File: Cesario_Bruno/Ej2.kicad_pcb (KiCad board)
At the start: 2 copper layers, 16 parts, among them P1 CONN_01X14, P2 CONN_01X14, U1 SN74LVC1GX04, U2 74HCT4053, U3 LTC5507, X1 XTAL

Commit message: Prueba de Ruteo PCB ambas capas. Finalizado.
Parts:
- C1, C2, C3, C4, C5, C6, R1, R2, R3, U1, U2, U3: moved to B.Cu
- PTC1: footprint Ej2:C_0805_HandSoldering -> Ej2:R_0805_HandSoldering; moved to B.Cu
- moved X1 60.9 mm to (163.8, 70.9), turned to 0 degrees
- moved R3 60.2 mm to (185.5, 86.0), turned to 270 degrees
- moved C2 59.2 mm to (182.6, 93.0), turned to 270 degrees
- moved P1 52.8 mm to (168.0, 80.0)
- moved C3 45.1 mm to (177.6, 91.5)
- moved C4 38.6 mm to (153.8, 84.4)
- moved PTC1 38.5 mm to (179.8, 86.3)
- moved C1 36.9 mm to (166.2, 92.7), turned to 180 degrees
- moved R1 36.2 mm to (173.5, 86.4)
- moved C5 35.8 mm to (166.1, 87.0)
- moved R2 35.3 mm to (160.4, 89.5)
- moved U2 34.2 mm to (152.9, 91.4), turned to 270 degrees
- moved U3 29.1 mm to (159.5, 84.0), turned to 270 degrees
- moved U1 25.3 mm to (158.1, 93.7)
- moved C6 23.8 mm to (172.0, 92.0), turned to 180 degrees
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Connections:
- PTC1 pad 1: (no net) -> /ArduinoCon/PTC
- PTC1 pad 2: (no net) -> GND
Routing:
- net GND: track 0.00 -> 74.0 mm, vias 0 -> 4
- net /ArduinoCon/ENVELOPE_IN: track 0.00 -> 70.6 mm, vias 0 -> 2
- net /ArduinoCon/FREQUENCY_IN: track 0.00 -> 53.6 mm
- net /OSC_DRIVER/Switch_IN-: track 0.00 -> 51.8 mm, vias 0 -> 2
- net +5V: track 0.00 -> 47.8 mm, vias 0 -> 2
- net +3V3: track 0.00 -> 40.4 mm, vias 0 -> 4
- net /SWITCH_ENVELOPE/xtal_N: track 0.00 -> 38.3 mm, vias 0 -> 1
- net /ArduinoCon/PTC: track 0.00 -> 32.4 mm, vias 0 -> 2
- net /SWITCH_ENVELOPE/xtal_P: track 0.00 -> 28.4 mm, vias 0 -> 1
- net Net-(R2-Pad1): track 0.00 -> 27.6 mm, vias 0 -> 2
- net /ArduinoCon/DIG_CONTROL: track 0.00 -> 25.7 mm, vias 0 -> 2
- net /OSC_DRIVER/Switch_IN+: track 0.00 -> 19.8 mm, vias 0 -> 2
- net Net-(C4-Pad1): track 0.00 -> 12.0 mm
- net Net-(C5-Pad2): track 0.00 -> 8.52 mm
- net Net-(C4-Pad2): track 0.00 -> 5.34 mm
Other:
- board outline added: 39.2 x 36 mm

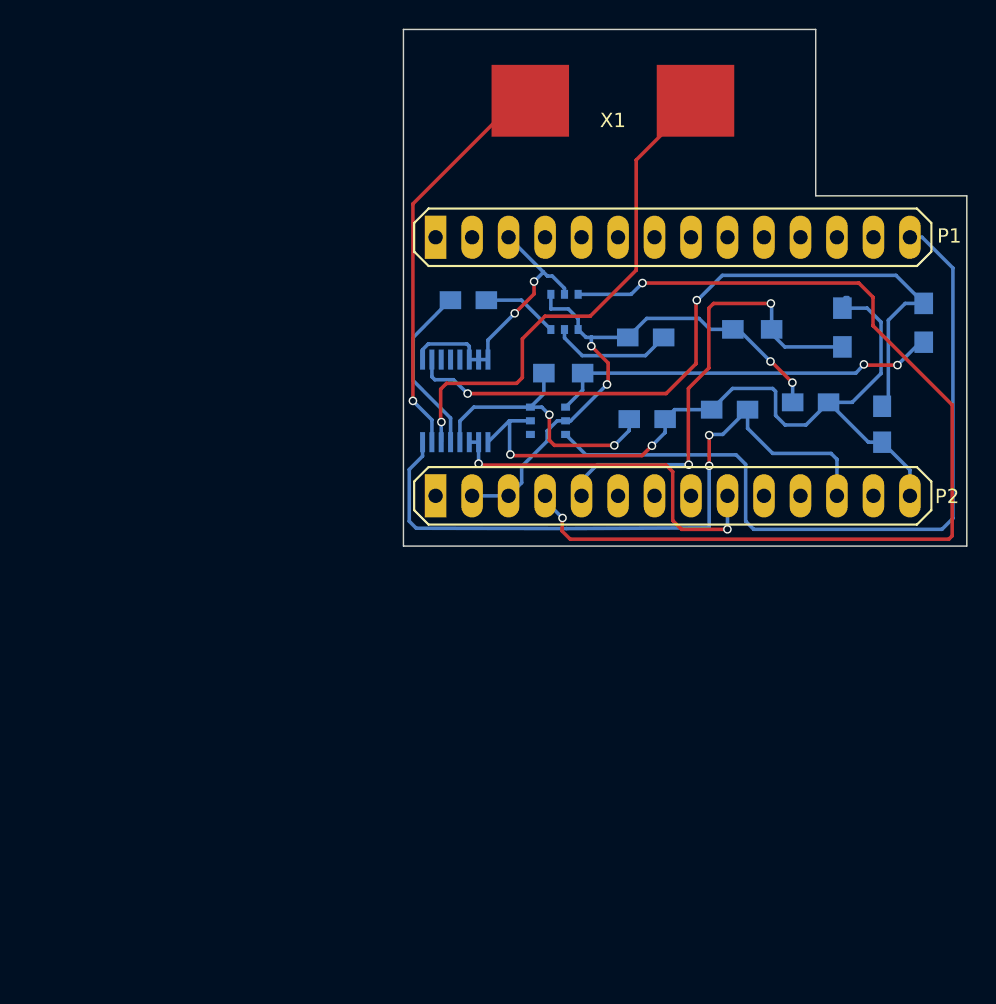
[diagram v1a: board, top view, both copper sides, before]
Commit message: Modificacion para inclusion de plantilla.
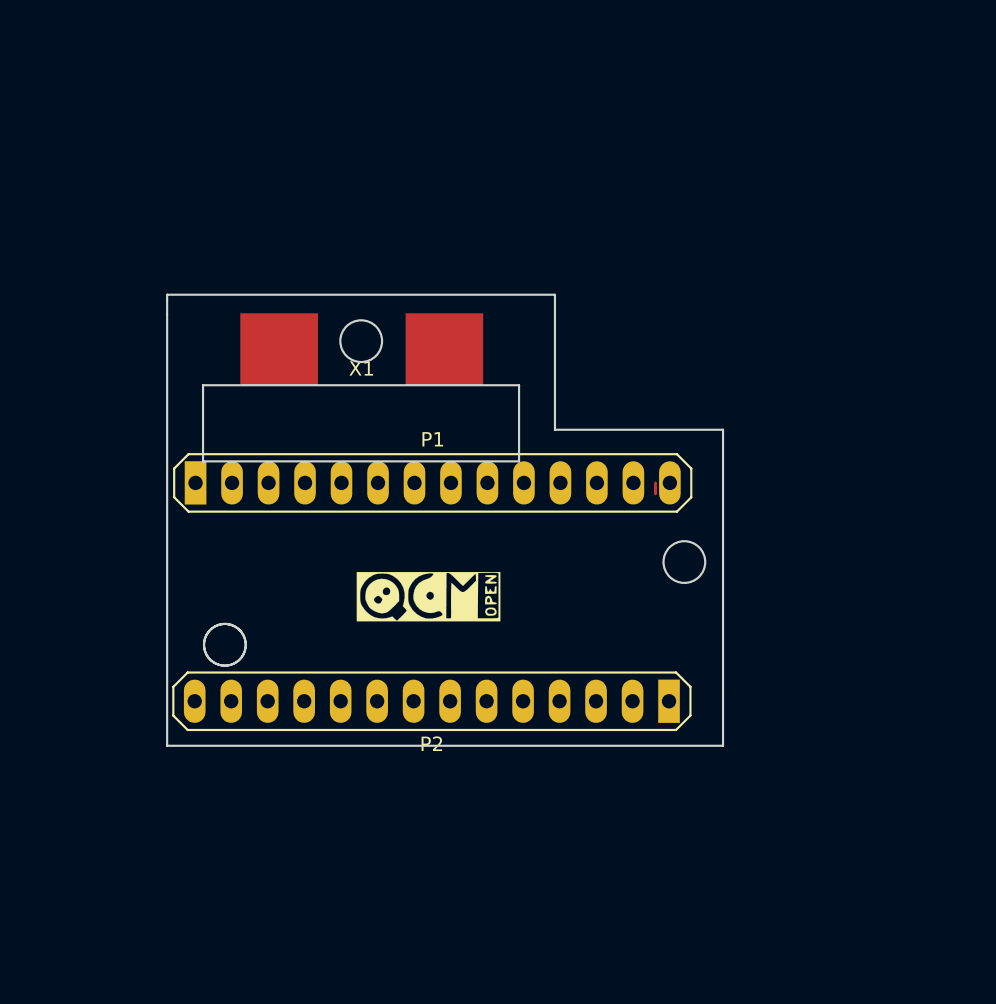
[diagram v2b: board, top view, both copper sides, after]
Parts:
- removed C1, C2: 33pF, Ej2:C_0805_HandSoldering
- removed C3, C6: 100nF, Ej2:C_0805_HandSoldering
- removed C4, C5: pF, Ej2:C_0805_HandSoldering
- removed PTC1: PTC_HandSoldering, Ej2:R_0805_HandSoldering
- removed R1, R3: 1K, Ej2:R_0805_HandSoldering
- removed R2: 2M2, Ej2:R_0805_HandSoldering
- removed U1: SN74LVC1GX04, Ej2:SOT-23-6
- removed U2: 74HCT4053, Ej2:TSSOP16
- removed U3: LTC5507, Ej2:SOT-23-6
- added G***: LOGO, OpenQCM:openQCM, F.Cu at (151.0, 105.0)
- P1, P2: footprint Ej2:PINHEAD1-14 -> OpenQCM:PINHEAD1-14
- X1: footprint Ej2:XTAL_con -> OpenQCM:XTAL_con
- moved X1 24.6 mm to (146.3, 88.2)
- moved P1 23.9 mm to (151.3, 97.1)
- moved P2 22.0 mm to (151.2, 112.3), turned to 180 degrees
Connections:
- P1 pad 1: Net-(P1-Pad1) -> (no net)
- P1 pad 10: Net-(P1-Pad10) -> (no net)
- P1 pad 11: Net-(P1-Pad11) -> (no net)
- P1 pad 12: Net-(P1-Pad12) -> (no net)
- P1 pad 13: Net-(P1-Pad13) -> (no net)
- P1 pad 14: /ArduinoCon/FREQUENCY_IN -> /Arduino/FREQUENCY_IN
- P1 pad 2: Net-(P1-Pad2) -> (no net)
- P1 pad 4: Net-(P1-Pad4) -> (no net)
- P1 pad 5: Net-(P1-Pad5) -> (no net)
- P1 pad 6: Net-(P1-Pad6) -> (no net)
- P1 pad 7: Net-(P1-Pad7) -> (no net)
- P1 pad 8: Net-(P1-Pad8) -> (no net)
- P1 pad 9: Net-(P1-Pad9) -> (no net)
- P2 pad 1: Net-(P2-Pad1) -> (no net)
- P2 pad 10: Net-(P2-Pad10) -> (no net)
- P2 pad 11: Net-(P2-Pad11) -> (no net)
- P2 pad 13: Net-(P2-Pad13) -> (no net)
- P2 pad 4: /ArduinoCon/ENVELOPE_IN -> /Arduino/ENVELOPE_IN
- P2 pad 5: /ArduinoCon/PTC -> /Arduino/PTC
- P2 pad 6: Net-(P2-Pad6) -> (no net)
- P2 pad 7: Net-(P2-Pad7) -> (no net)
- P2 pad 8: Net-(P2-Pad8) -> (no net)
- P2 pad 9: /ArduinoCon/DIG_CONTROL -> /Arduino/DIG_CONTROL
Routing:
- net GND: track 74.0 -> 0.00 mm, vias 4 -> 0
- net /ArduinoCon/ENVELOPE_IN: track 70.6 -> 0.00 mm, vias 2 -> 0
- net /ArduinoCon/FREQUENCY_IN: track 53.6 -> 0.00 mm
- net /OSC_DRIVER/Switch_IN-: track 51.8 -> 0.00 mm, vias 2 -> 0
- net +5V: track 47.8 -> 0.00 mm, vias 2 -> 0
- net +3V3: track 40.4 -> 0.00 mm, vias 4 -> 0
- net /SWITCH_ENVELOPE/xtal_N: track 38.3 -> 0.00 mm, vias 1 -> 0
- net /ArduinoCon/PTC: track 32.4 -> 0.00 mm, vias 2 -> 0
- net /SWITCH_ENVELOPE/xtal_P: track 28.4 -> 0.00 mm, vias 1 -> 0
- net Net-(R2-Pad1): track 27.6 -> 0.00 mm, vias 2 -> 0
- net /ArduinoCon/DIG_CONTROL: track 25.7 -> 0.00 mm, vias 2 -> 0
- net /OSC_DRIVER/Switch_IN+: track 19.8 -> 0.00 mm, vias 2 -> 0
- net Net-(C4-Pad1): track 12.0 -> 0.00 mm
- net Net-(C5-Pad2): track 8.52 -> 0.00 mm
- net Net-(C4-Pad2): track 5.34 -> 0.00 mm
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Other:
- board size 39.2 x 36 mm -> 38.7 x 31.4 mm
- net class Default: trace_width 0.25 -> 0.2032
- net class PW added: clearance 0.2, trace_width 0.5, via_dia 0.6, via_drill 0.4
- rule pad_to_mask_clearance: 0 -> 0.2
- rule trace_min: 0.2 -> 0.2032

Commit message: Fin Clase 3. Generacion Nuevo PCB y Ruteo. Capa de Cobre. Archivos Gerber y Visualización.
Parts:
- removed the G*** at (151.0, 105.0)
- added C1: 33pF, Ej2:C_0603_HandSoldering, B.Cu at (145.8, 104.1)
- added C2: 33pF, Ej2:C_0603_HandSoldering, B.Cu at (155.3, 108.1)
- added C3: 100nF, Ej2:C_0603_HandSoldering, B.Cu at (148.4, 100.7)
- added C4: pF, Ej2:C_0603_HandSoldering, B.Cu at (158.9, 108.2)
- added C5: pF, Ej2:C_0603_HandSoldering, B.Cu at (162.6, 105.7)
- added C6: 100nF, Ej2:C_0603_HandSoldering, B.Cu at (162.8, 109.3)
- added G***: LOGO, Ej2:openQCM, F.Cu at (151.4, 103.0)
- added PTC1: PTC_HandSoldering, Ej2:R_0805_HandSoldering, B.Cu at (153.0, 103.7)
- added R1: 1K, Ej2:R_0805_HandSoldering, B.Cu at (157.4, 102.8)
- added R2: 2M2, Ej2:R_0805_HandSoldering, B.Cu at (145.9, 109.0)
- added R3: 1K, Ej2:R_0805_HandSoldering, B.Cu at (151.9, 109.0)
- added U1: SN74LVC1GX04, Ej2:SOT-23-6, B.Cu at (162.2, 102.7)
- added U2: 74HCT4053, Ej2:TSSOP16, B.Cu at (141.3, 103.7)
- added U3: LTC5507, Ej2:SOT-23-6, B.Cu at (168.0, 108.3)
- P1, P2: footprint OpenQCM:PINHEAD1-14 -> Ej2:PINHEAD1-14
- X1: footprint OpenQCM:XTAL_con -> Ej2:XTAL_con; moved to B.Cu
- moved X1 2.16 mm to (147.6, 86.4)
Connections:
- P1 pad 1: (no net) -> Net-(P1-Pad1)
- P1 pad 10: (no net) -> Net-(P1-Pad10)
- P1 pad 11: (no net) -> Net-(P1-Pad11)
- P1 pad 12: (no net) -> Net-(P1-Pad12)
- P1 pad 13: (no net) -> Net-(P1-Pad13)
- P1 pad 14: /Arduino/FREQUENCY_IN -> /ArduinoCon/FREQUENCY_IN
- P1 pad 2: (no net) -> Net-(P1-Pad2)
- P1 pad 4: (no net) -> Net-(P1-Pad4)
- P1 pad 5: (no net) -> Net-(P1-Pad5)
- P1 pad 6: (no net) -> Net-(P1-Pad6)
- P1 pad 7: (no net) -> Net-(P1-Pad7)
- P1 pad 8: (no net) -> Net-(P1-Pad8)
- P1 pad 9: (no net) -> Net-(P1-Pad9)
- P2 pad 1: (no net) -> Net-(P2-Pad1)
- P2 pad 10: (no net) -> Net-(P2-Pad10)
- P2 pad 11: (no net) -> Net-(P2-Pad11)
- P2 pad 13: (no net) -> Net-(P2-Pad13)
- P2 pad 4: /Arduino/ENVELOPE_IN -> /ArduinoCon/ENVELOPE_IN
- P2 pad 5: /Arduino/PTC -> /ArduinoCon/PTC
- P2 pad 6: (no net) -> Net-(P2-Pad6)
- P2 pad 7: (no net) -> Net-(P2-Pad7)
- P2 pad 8: (no net) -> Net-(P2-Pad8)
- P2 pad 9: /Arduino/DIG_CONTROL -> /ArduinoCon/DIG_CONTROL
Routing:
- net /SWITCH_ENVELOPE/xtal_P: track 0.00 -> 55.6 mm
- net +3V3: track 0.00 -> 49.3 mm
- net /SWITCH_ENVELOPE/xtal_N: track 0.00 -> 48.8 mm
- net GND: track 0.00 -> 37.5 mm, vias 0 -> 4
- net +5V: track 0.00 -> 35.3 mm
- net Net-(R2-Pad1): track 0.00 -> 31.8 mm, vias 0 -> 2
- net Net-(C4-Pad1): track 0.00 -> 30.4 mm
- net /OSC_DRIVER/Switch_IN+: track 0.00 -> 27.9 mm, vias 0 -> 4
- net /OSC_DRIVER/Switch_IN-: track 0.00 -> 19.5 mm, vias 0 -> 2
- net /ArduinoCon/PTC: track 0.00 -> 15.9 mm, vias 0 -> 2
- net Net-(C4-Pad2): track 0.00 -> 10.9 mm
- net /ArduinoCon/DIG_CONTROL: track 0.00 -> 10.3 mm
- net Net-(C5-Pad2): track 0.00 -> 10.0 mm
- net /ArduinoCon/ENVELOPE_IN: track 0.00 -> 9.85 mm
- net /ArduinoCon/FREQUENCY_IN: track 0.00 -> 7.88 mm
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- added copper zone on B.Cu, net (none)
- added copper zone on B.Cu, net GND
- added copper zone on F.Cu, net GND
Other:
- net class Default: trace_width 0.2032 -> 0.2; via_drill 0.4 -> 0.3
- net class PW: via_drill 0.4 -> 0.3
- rule trace_min: 0.2032 -> 0.2
- rule via_min_size: 0.4 -> 0.6
